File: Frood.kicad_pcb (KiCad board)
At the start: 2 copper layers, 17.8 x 33.5 mm, 39 parts, among them J1 Left, J2 Right, J3 Bottom, SW1 RESET, SW2 BOOT, U1 RP2040, U2 W25Q32JWUUIQ, U3 SPX3819M5-L-3-3/TR, Y1 X322512MSB4SI

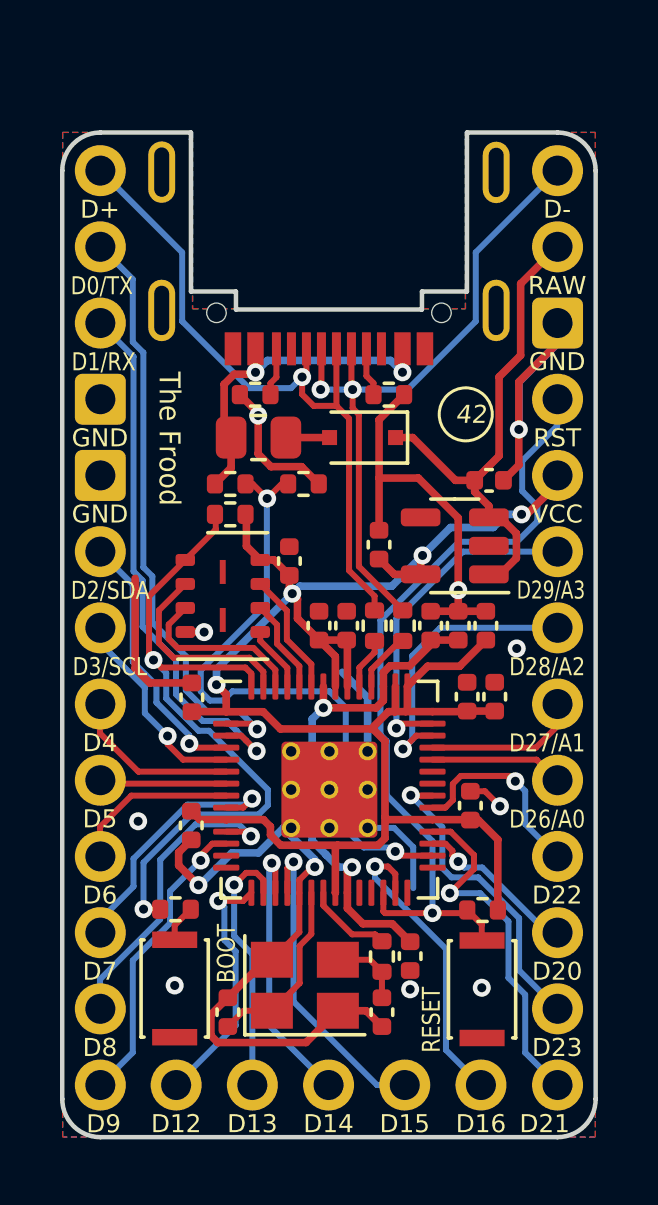
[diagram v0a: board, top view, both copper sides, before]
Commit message: Rev4 update
* Use correctly-specced 16 Mbit QSPI flash
* Switch to fully mid-mounted GT-USB-7014C USB-C socket and 1.6 mm PCB
* Improve pin labels
* Improve routing
* Update the README with version history
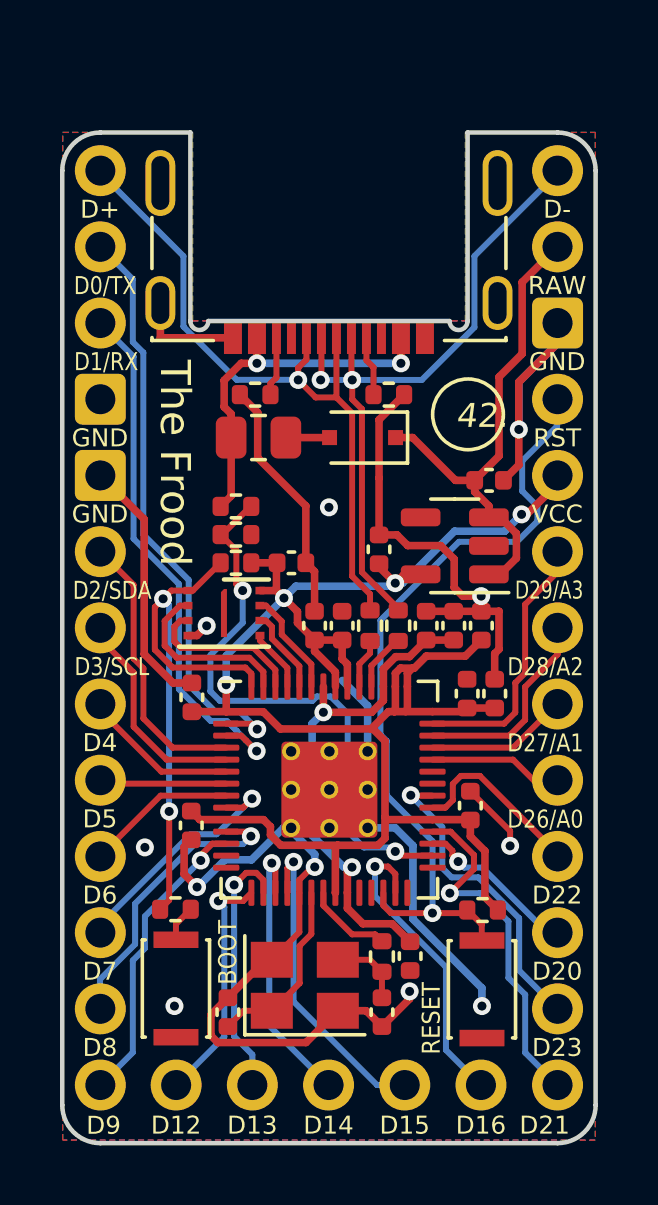
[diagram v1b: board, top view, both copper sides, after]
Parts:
- U2: value W25Q32JWUUIQ -> ZD25WQ16BUIGR; footprint 42keebs:USON-8_4x3mm_P0.8mm -> 42keebs:DFN-8-1EP_3x2mm_P0.5mm_EP0.2x1.6mm
- USB1: value HRO-TYPE-C-31-M-14 -> GT-USB-7014C; footprint 42keebs:TYPE-C-31-M-14-PiMicro -> 42keebs:Molex-216990_GCT-USB45xx_HRO-TYPE-C-31-M-13x-PiMicro
- moved R12 2.81 mm to (123.2, 68.4)
- moved USB1 1.73 mm to (126.3, 55.5)
- moved R7 1.63 mm to (123.2, 69.3)
- moved LOGO1 0.85 mm to (126.3, 67.5)
- moved R11 0.77 mm to (123.2, 67.4)
- moved U2 0.57 mm to (122.8, 71.0)
- moved C2 0.16 mm to (128.0, 68.9)
- moved C12 0.15 mm to (126.7, 71.4)
- moved C14 0.15 mm to (125.8, 71.4)
- moved C6 0.15 mm to (129.5, 71.4)
- moved C7 0.15 mm to (130.5, 71.4)
- moved C9 0.15 mm to (131.4, 71.4)
- moved R4 0.15 mm to (127.7, 71.4)
- moved R3 0.15 mm to (128.6, 71.4)
- moved C10 0.10 mm to (131.8, 73.7)
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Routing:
- net GND: track 61.9 -> 81.6 mm, vias 12 -> 11
- net /QSPI_SS: track 23.4 -> 18.8 mm
- net /D28/A2: track 9.62 -> 6.82 mm, vias 1 -> 0
- net /D29/A3: track 11.2 -> 8.86 mm, vias 1 -> 0
- net Net-(R11-Pad1): track 21.6 -> 19.5 mm
- net /QSPI_SD1: track 6.71 -> 5.96 mm
- net /D8: track 10.4 -> 9.67 mm
- net /D7: track 8.69 -> 8.06 mm
- net VBUS: track 11.6 -> 12.3 mm
- net /QSPI_SD3: track 4.12 -> 3.53 mm
- net /D22: track 6.68 -> 6.09 mm, vias 1 -> 0
- net /D6: track 5.62 -> 5.05 mm
- net /D2/SDA: track 8.92 -> 9.32 mm, vias 1 -> 0
- net /D3/SCL: track 6.98 -> 7.30 mm, vias 1 -> 0
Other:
- board size 17.8 x 33.5 mm -> 17.8 x 33.7 mm
- board text added: "The Frood rev4 42keebs.eu 2022"
- board text removed: "The Frood rev3 42Keebs.eu 2022"

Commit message: Improve USB socket position; add boot/reset pads on the bottom
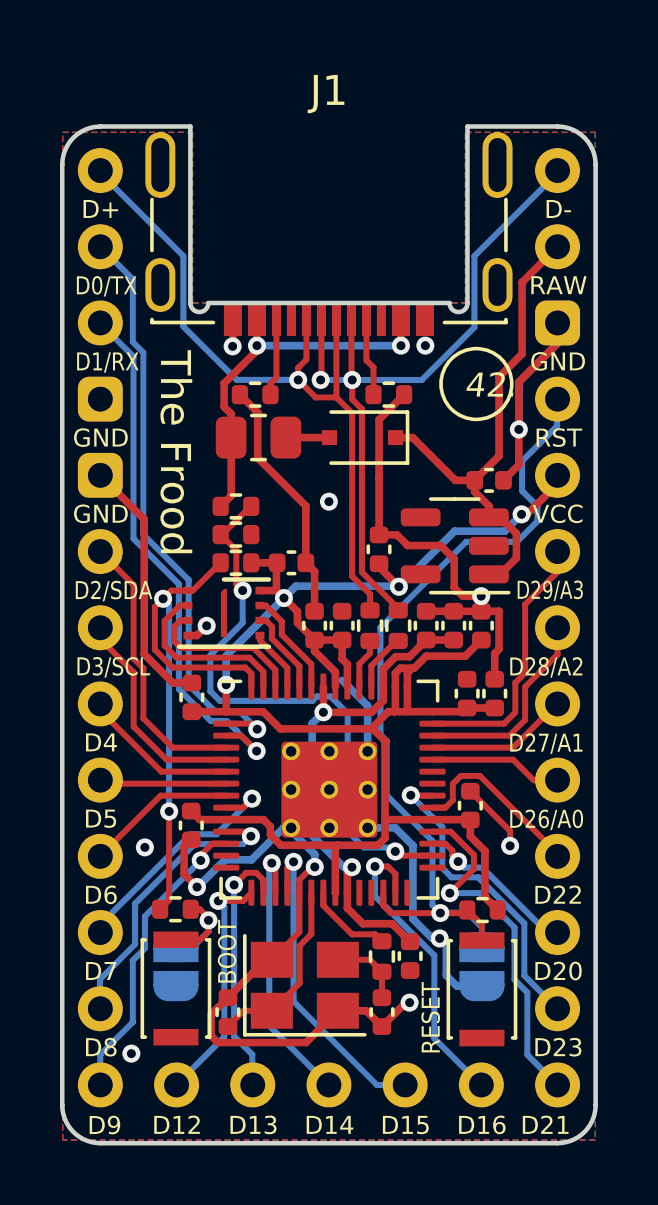
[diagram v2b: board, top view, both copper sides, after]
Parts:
- removed J2: Right, 42keebs:PinHeader_1x13_P2.54mm_Vertical_ProMicro-Right
- removed J3: Bottom, 42keebs:PinHeader_1x05_P2.54mm_Vertical_Plain
- added JP1: RESET, Jumper:SolderJumper-2_P1.3mm_Open_RoundedPad1.0x1.5mm, B.Cu at (131.4, 82.8)
- added JP2: BOOT, Jumper:SolderJumper-2_P1.3mm_Open_RoundedPad1.0x1.5mm, B.Cu at (121.2, 82.8)
- J1: value Left -> Conn_02x13+5; footprint 42keebs:PinHeader_1x13_P2.54mm_Vertical_ProMicro-Left -> 42keebs:PinHeader_2x13+5_P2.54mm_Vertical_Elite-C
- moved J1 7.62 mm to (126.3, 56.2)
- moved USB1 0.60 mm to (126.3, 54.9)
- moved LOGO1 0.19 mm to (126.3, 67.3)
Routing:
- net GND: track 81.6 -> 78.6 mm, vias 11 -> 13
- net /~{USB_BOOT}: track 1.22 -> 4.02 mm, vias 0 -> 1
- net /~{RESET}: track 26.4 -> 28.7 mm
- net /D-: track 23.4 -> 24.6 mm
- net /D+: track 23.5 -> 24.7 mm
- net Net-(R1-Pad2): track 1.99 -> 2.59 mm
- net Net-(R2-Pad2): track 1.98 -> 2.58 mm
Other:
- board size 17.8 x 33.7 mm -> 17.8 x 33.9 mm
- board text added: "Frood rev4b 42keebs.eu 2022"
- board text removed: "D+"
- board text removed: "D-"
- board text removed: "D0/TX"
- board text removed: "D1/RX"
- board text removed: "D12"
- board text removed: "D13"
- board text removed: "D14"
- board text removed: "D15"
- board text removed: "D16"
- board text removed: "D2/SDA"
- board text removed: "D20"
- board text removed: "D21"
- board text removed: "D22"
- board text removed: "D23"
- board text removed: "D26/A0"
- board text removed: "D27/A1"
- board text removed: "D28/A2"
- board text removed: "D29/A3"
- board text removed: "D3/SCL"
- board text removed: "D4"
- board text removed: "D5"
- board text removed: "D6"
- board text removed: "D7"
- board text removed: "D8"
- board text removed: "D9"
- board text removed: "GND"
- board text removed: "RAW"
- board text removed: "RST"
- board text removed: "The Frood rev4 42keebs.eu 2022"
- board text removed: "VCC"

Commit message: Rev5 update
* Use a smaller crystal to get some valuable space back
* Add an orange indicator LED on pin GPIO17
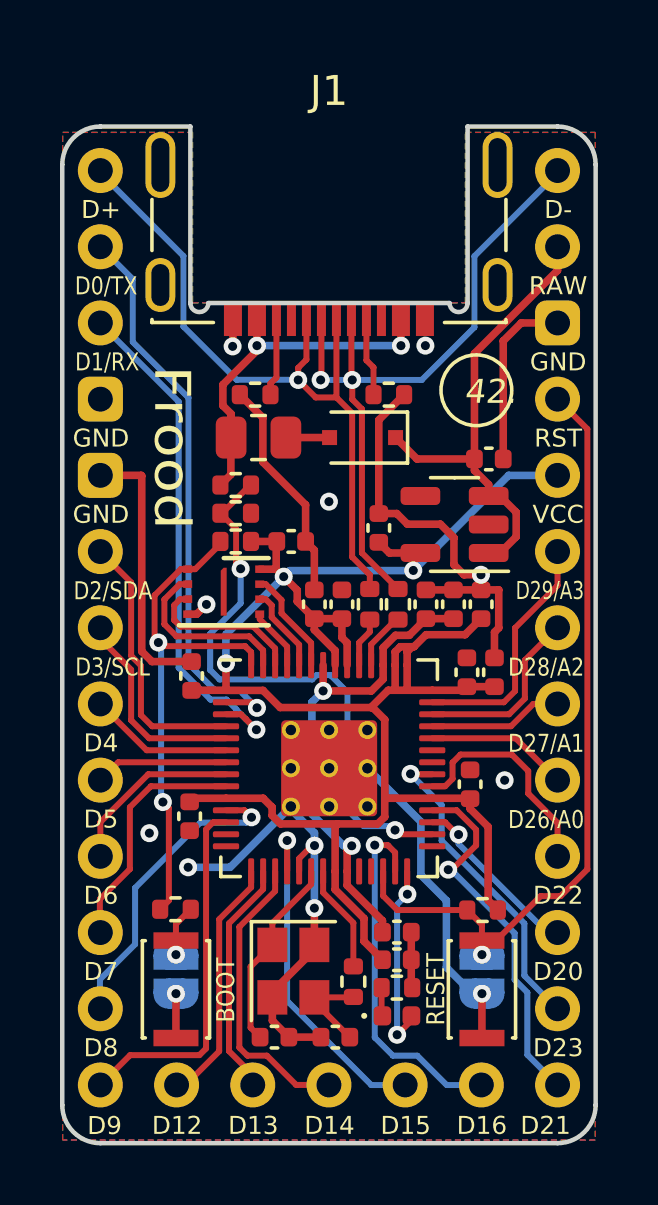
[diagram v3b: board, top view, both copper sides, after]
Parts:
- added C17: 100n, Capacitor_SMD:C_0402_1005Metric, F.Cu at (128.6, 82.6)
- added D2: LED, LED_SMD:LED_0402_1005Metric, F.Cu at (128.6, 84.4)
- added R9: 1k, Resistor_SMD:R_0402_1005Metric, F.Cu at (128.6, 83.5)
- Y1: value X322512MSB4SI -> TXM12M0004252LBCEO00T; footprint Crystal:Crystal_SMD_3225-4Pin_3.2x2.5mm -> Crystal:Crystal_SMD_2520-4Pin_2.5x2.0mm
- moved C3 1.76 mm to (124.5, 85.1), turned to 0 degrees
- moved C4 1.76 mm to (126.5, 85.1), turned to 180 degrees
- moved R5 1.27 mm to (127.1, 83.3)
- moved C8 0.91 mm to (128.6, 81.6), turned to 0 degrees
- moved C16 0.71 mm to (131.0, 76.7)
- moved C13 0.71 mm to (121.7, 73.1)
- moved C5 0.71 mm to (125.0, 68.6)
- moved R12 0.71 mm to (123.2, 67.7)
- moved R7 0.71 mm to (123.2, 68.6)
- moved U1 0.71 mm to (126.3, 76.2)
- moved U3 0.71 mm to (130.5, 68.0)
- moved C11 0.71 mm to (130.9, 73.0)
- moved C7 0.71 mm to (130.5, 70.7)
- moved R3 0.71 mm to (128.6, 70.7)
- moved C2 0.71 mm to (128.0, 68.2)
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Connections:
- U1 pad 28: unconnected-(U1-Pad28) -> /LED
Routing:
- net GND: track 78.6 -> 67.6 mm, vias 13 -> 12
- net /LED: track 0.00 -> 6.42 mm, vias 0 -> 2
- net +3V3: track 62.1 -> 66.2 mm, vias 4 -> 3
- net /~{RESET}: track 28.7 -> 26.1 mm
- net /~{USB_BOOT}: track 4.02 -> 1.72 mm
- net /D9: track 10.1 -> 12.1 mm, vias 1 -> 0
- net /D16: track 10.2 -> 12.0 mm
- net /D22: track 6.09 -> 7.43 mm
- net /QSPI_SS: track 18.8 -> 17.4 mm
- net /RAW: track 16.7 -> 15.7 mm
- net Net-(D2-Pad1): track 0.00 -> 0.95 mm
- net /D6: track 5.05 -> 5.99 mm
- net /D15: track 10.6 -> 11.5 mm
- net /D-: track 24.6 -> 23.9 mm
- net /D0/TX: track 19.8 -> 19.1 mm
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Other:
- board text added: "Frood"
- board text added: "Frood rev5 42keebs.eu 2022"
- board text removed: "Frood rev4b 42keebs.eu 2022"
- board text removed: "The Frood"
